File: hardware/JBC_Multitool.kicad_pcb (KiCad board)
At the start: 2 copper layers, 122 x 93 mm, 52 parts, among them J1 Screw_Terminal_01x02, J2 Mini XLR6, J4 Mini XLR6, J5 Mini XLR6, J6 Binder 09-0998-00-05, J7 Binder 09-0998-00-05, K1 RT314005, K10 HF49FD_005-1H12T, K11 HF49FD_005-1H12T, K12 HF49FD_005-1H12T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

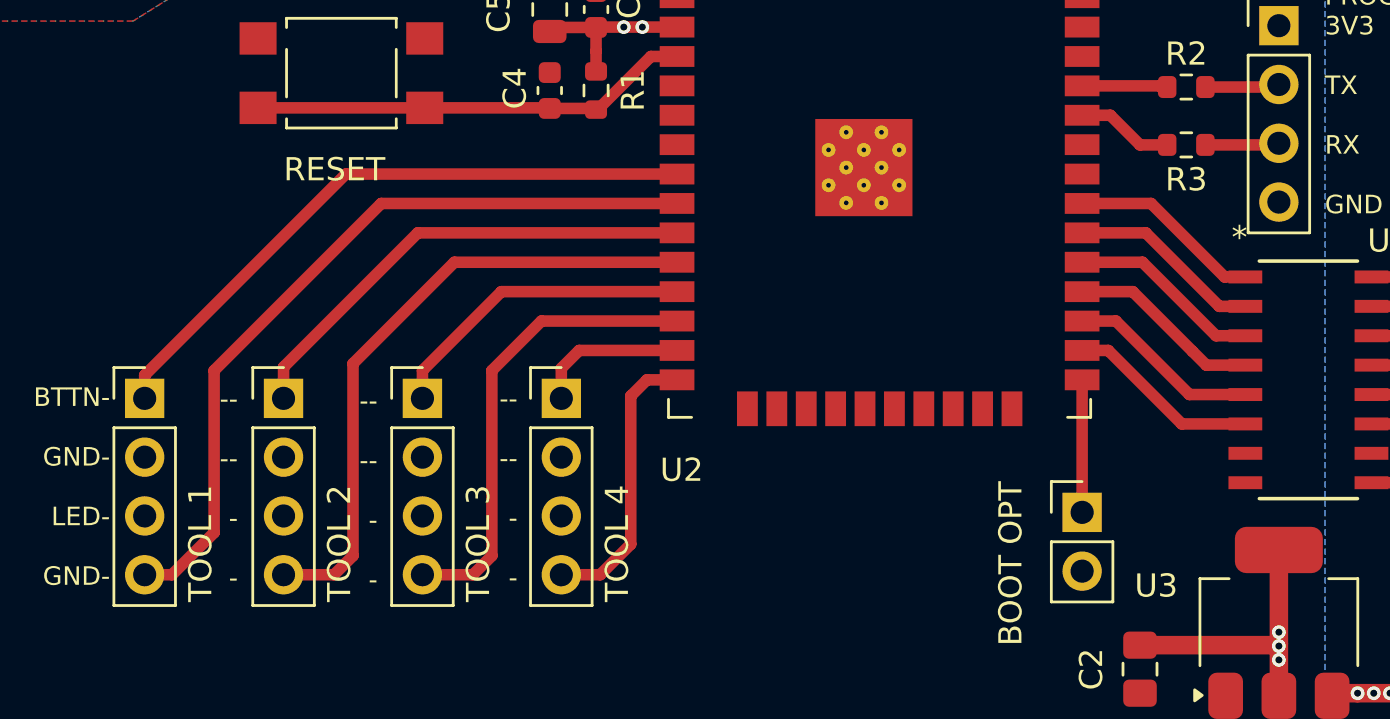
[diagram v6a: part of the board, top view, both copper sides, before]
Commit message: Add files via upload
PCB und Schaltplan überarbeitet.
GPIO5 & GPIO14 jetzt „not connected“, da diese GPIOs beim Boot auf HIGH gesetzt werden und die Relais und die LED anschalteten.
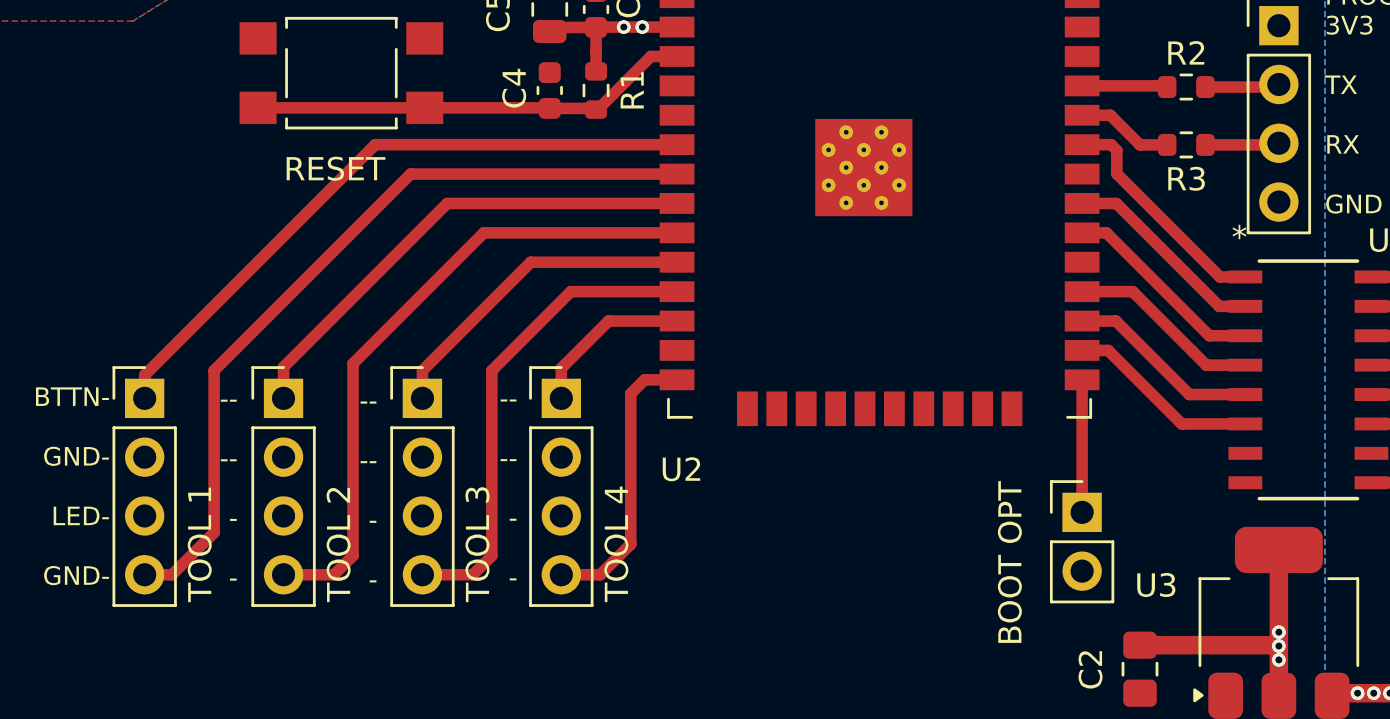
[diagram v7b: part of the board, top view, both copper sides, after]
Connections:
- J2 pad 3: (no net) -> unconnected-(J2-P3-Pad3)
- J4 pad 3: (no net) -> unconnected-(J4-P3-Pad3)
- J4 pad 4: (no net) -> unconnected-(J4-P3-Pad4)
- J5 pad 3: (no net) -> unconnected-(J5-P3-Pad3)
- U2 pad 10: /SELECT_TOOL_LED_2 -> /SELECT_TOOL_3
- U2 pad 11: /SELECT_TOOL_3 -> /SELECT_TOOL_LED_3
- U2 pad 12: /SELECT_TOOL_LED_3 -> /SELECT_TOOL_4
- U2 pad 13: /SELECT_TOOL_4 -> unconnected-(U2-IO14-Pad13)
- U2 pad 29: /TOOL_1_CTRL -> unconnected-(U2-IO5-Pad29)
- U2 pad 30: /TOOL_SENSOR_CTRL -> /TOOL_1_CTRL
- U2 pad 31: /TOOL_POWER_CTRL -> /TOOL_SENSOR_CTRL
- U2 pad 33: unconnected-(U2-IO21-Pad33) -> /TOOL_POWER_CTRL
- U2 pad 6: unconnected-(U2-IO34-Pad6) -> /SELECT_TOOL_1
- U2 pad 7: /SELECT_TOOL_1 -> /SELECT_TOOL_LED_1
- U2 pad 8: /SELECT_TOOL_LED_1 -> /SELECT_TOOL_2
- U2 pad 9: /SELECT_TOOL_2 -> /SELECT_TOOL_LED_2
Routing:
- net /TOOL_POWER_CTRL: track 8.37 -> 10.0 mm
- net /SELECT_TOOL_LED_1: track 33.7 -> 34.3 mm
- net /TOOL_1_CTRL: track 8.37 -> 8.89 mm
- net /SELECT_TOOL_LED_2: track 27.5 -> 28.0 mm
- net /SELECT_TOOL_3: track 13.6 -> 14.1 mm
- net /TOOL_SENSOR_CTRL: track 8.37 -> 8.89 mm
- net /SELECT_TOOL_LED_3: track 20.2 -> 20.8 mm
- net /SELECT_TOOL_2: track 20.8 -> 21.3 mm
- net /SELECT_TOOL_1: track 27.6 -> 28.1 mm
- net /SELECT_TOOL_4: track 6.62 -> 7.14 mm
